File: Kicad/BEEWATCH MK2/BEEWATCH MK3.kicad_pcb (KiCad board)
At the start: 2 copper layers, 40.3 x 39.7 mm, 113 parts, among them IC1 LTC3549EDCB#TRMPBF, J1 USB_C_Receptacle_USB2.0, J3 Conn_02x06_Odd_Even, Q1 DMG6968U, Q2 DMG6968U, Q3 DMP1045U-7, Q4 DMG6968U, Q5 BSS138, Q6 BSS138, Q7 BSS138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

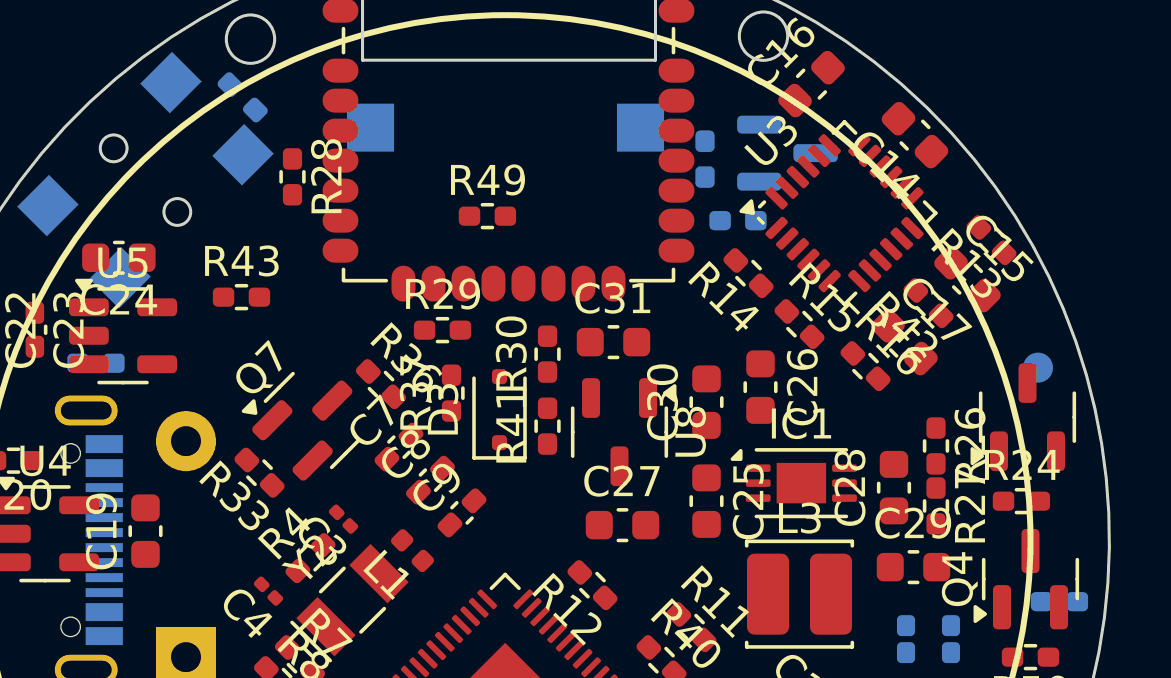
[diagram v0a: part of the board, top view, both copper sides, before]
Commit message: Added Buzzer flyback diode
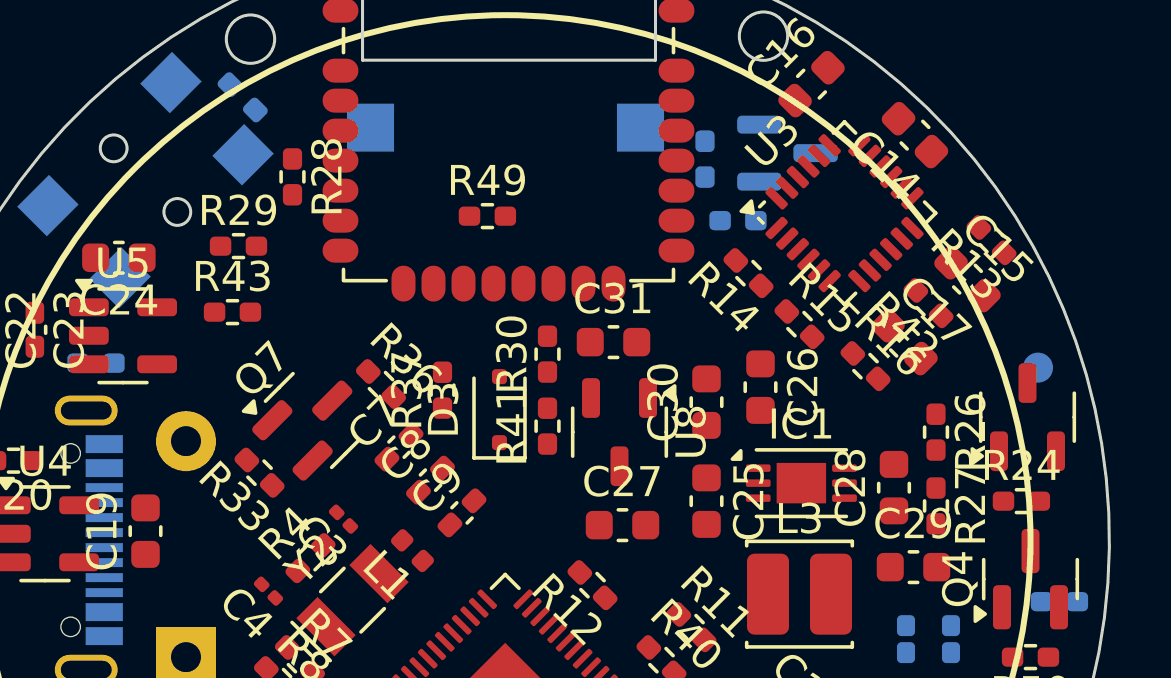
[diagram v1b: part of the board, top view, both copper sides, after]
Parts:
- moved R29 7.35 mm to (141.1, 95.2)
- moved R43 0.58 mm to (140.9, 97.4)
- moved R26 0.46 mm to (164.3, 101.4)
- moved R37 0.32 mm to (147.9, 100.0)
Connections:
- Q5 pad 1: GNSS_+1V8 -> /RYS8830/GNSS_+1.8V
- Q6 pad 1: GNSS_+1V8 -> /RYS8830/GNSS_+1.8V
- Q7 pad 1: GNSS_+1V8 -> /RYS8830/GNSS_+1.8V
- R31 pad 2: GNSS_+1V8 -> /RYS8830/GNSS_+1.8V
- R32 pad 2: GNSS_+1V8 -> /RYS8830/GNSS_+1.8V
- R33 pad 2: GNSS_+1V8 -> /RYS8830/GNSS_+1.8V
- U7 pad 14: GNSS_+1V8 -> /RYS8830/GNSS_+1.8V
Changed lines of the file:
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@@
 			(layers "F.Cu" "F.Paste" "F.Mask")
 			(roundrect_rratio 0.25)
-			(net 122 "GNSS_+1V8")
+			(net 87 "/RYS8830/GNSS_+1.8V")
 			(pinfunction "G")
 			(pintype "input")
@@
 			(layers "F.Cu" "F.Paste" "F.Mask")
 			(roundrect_rratio 0.25)
-			(net 122 "GNSS_+1V8")
+			(net 87 "/RYS8830/GNSS_+1.8V")
 			(pinfunction "G")
 			(pintype "input")
@@
 			(layers "F.Cu" "F.Paste" "F.Mask")
 			(roundrect_rratio 0.25)
-			(net 122 "GNSS_+1V8")
+			(net 87 "/RYS8830/GNSS_+1.8V")
 			(pintype "passive")
 		)
@@
 	(footprint "Resistor_SMD:R_0402_1005Metric_Pad0.72x0.64mm_HandSolder"
 		(layer "F.Cu")
-		(at 147.9 98)
+		(at 141.1 95.2)
 		(descr "Resistor SMD 0402 (1005 Metric), square (rectangular) end terminal, IPC_7351 nominal with elongated pad for handsoldering. (Body size source: IPC-SM-782 page 72, https://www.pcb-3d.com/wordpress/wp-content/uploads/ipc-sm-782a_amendment_1_and_2.pdf), generated with kicad-footprint-generator")
 		(tags "resistor handsolder")
@@
 			(layers "F.Cu" "F.Paste" "F.Mask")
 			(roundrect_rratio 0.25)
-			(net 122 "GNSS_+1V8")
+			(net 87 "/RYS8830/GNSS_+1.8V")
 			(pinfunction "G")
 			(pintype "input")
@@
 			(layers "F.Cu" "F.Paste" "F.Mask")
 			(roundrect_rratio 0.25)
-			(net 122 "GNSS_+1V8")
+			(net 87 "/RYS8830/GNSS_+1.8V")
 			(pintype "passive")
 		)
@@
 			(size 0.8 1.2)
 			(layers "F.Cu" "F.Paste" "F.Mask")
-			(net 122 "GNSS_+1V8")
+			(net 87 "/RYS8830/GNSS_+1.8V")
 			(pinfunction "SYSTEM0")
 			(pintype "passive")
@@
 	(footprint "Resistor_SMD:R_0402_1005Metric_Pad0.72x0.64mm_HandSolder"
 		(layer "F.Cu")
-		(at 141.2 96.9)
+		(at 140.9 97.4)
 		(descr "Resistor SMD 0402 (1005 Metric), square (rectangular) end terminal, IPC_7351 nominal with elongated pad for handsoldering. (Body size source: IPC-SM-782 page 72, https://www.pcb-3d.com/wordpress/wp-content/uploads/ipc-sm-782a_amendment_1_and_2.pdf), generated with kicad-footprint-generator")
 		(tags "resistor handsolder")
@@
 	(footprint "Resistor_SMD:R_0402_1005Metric_Pad0.72x0.64mm_HandSolder"
 		(layer "F.Cu")
-		(at 148.2 100.1 90)
+		(at 147.9 100 90)
 		(descr "Resistor SMD 0402 (1005 Metric), square (rectangular) end terminal, IPC_7351 nominal with elongated pad for handsoldering. (Body size source: IPC-SM-782 page 72, https://www.pcb-3d.com/wordpress/wp-content/uploads/ipc-sm-782a_amendment_1_and_2.pdf), generated with kicad-footprint-generator")
 		(tags "resistor handsolder")
@@
 			(layers "F.Cu" "F.Paste" "F.Mask")
 			(roundrect_rratio 0.25)
-			(net 122 "GNSS_+1V8")
+			(net 87 "/RYS8830/GNSS_+1.8V")
 			(pintype "passive")
 		)
@@
 	(footprint "Resistor_SMD:R_0402_1005Metric_Pad0.72x0.64mm_HandSolder"
 		(layer "F.Cu")
-		(at 164.35 101.86 -90)
+		(at 164.35 101.4 -90)
 		(descr "Resistor SMD 0402 (1005 Metric), square (rectangular) end terminal, IPC_7351 nominal with elongated pad for handsoldering. (Body size source: IPC-SM-782 page 72, https://www.pcb-3d.com/wordpress/wp-content/uploads/ipc-sm-782a_amendment_1_and_2.pdf), generated with kicad-footprint-generator")
 		(tags "resistor handsolder")

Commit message: Updated with sub module lib
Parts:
- added D4: ZLLS410TA, Diode_SMD:D_SOD-323F, F.Cu at (174.9, 103.0)
- added R25: 1M, Resistor_SMD:R_0402_1005Metric_Pad0.72x0.64mm_HandSolder, F.Cu at (174.4, 107.5)
- AE1: footprint Project:ANT -> ANTENNA:RYS8830_ANT
- BT1: footprint Project:WLY902025 -> BATTERY:WLY902025
- BZ1: footprint Project:CL9032A-CLDZ-SMD Passive Buzzer -> SM_BUZZER:CL9032A-CLDZ-SMD Passive Buzzer
- D1: footprint Project:XL-0807RGBC-WS2812B -> SM_LED:XL-0807RGBC-WS2812B
- SW1, SW2: footprint Project:Tact Switch-TK-074-4 Pin SMD -> SM_SWITCH:Tact Switch-TK-074-4 Pin SMD
- U7: footprint Project:RYS8830 -> REYAS:RYS8830
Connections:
- net /Battery&BMS/+3V3 renamed /Battery&BMS/+3V3_IN
- C22 pad 1: +VBAT -> /Battery&BMS/+VBAT_IN
- C23 pad 1: +VBAT -> /Battery&BMS/+VBAT_IN
- R48 pad 2: +VBAT -> /Battery&BMS/+VBAT_IN
- U5 pad 1: +VBAT -> /Battery&BMS/+VBAT_IN
- U5 pad 3: +VBAT -> /Battery&BMS/+VBAT_IN

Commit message: Lib Integration almost done
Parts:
- AE1: footprint ANTENNA:RYS8830_ANT -> ANTENNA:ESP32_ZERO_ANT
- D4: moved to B.Cu
- moved D4 23.4 mm to (156.5, 88.6), turned to 90 degrees
- moved R3 0.58 mm to (141.8, 90.1)

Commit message: minor change in ESP32
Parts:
- added R51: 0, Resistor_SMD:R_0402_1005Metric_Pad0.72x0.64mm_HandSolder, F.Cu at (144.9, 115.6)
- added R52: 0, Resistor_SMD:R_0402_1005Metric_Pad0.72x0.64mm_HandSolder, F.Cu at (145.9, 116.6)
- U1: value ESP32-S3 -> ESP32-S3FH4R2
- moved R25 14.1 mm to (160.5, 109.7), turned to -45 degrees
- moved D1 4.10 mm to (167.1, 111.1)
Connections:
- U1 pad 51: unconnected-(U1-GPIO45-Pad51) -> Net-(U1-GPIO45)
- U1 pad 52: unconnected-(U1-GPIO46-Pad52) -> Net-(U1-GPIO46)
